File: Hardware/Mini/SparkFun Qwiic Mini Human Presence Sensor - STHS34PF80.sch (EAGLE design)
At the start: 29 parts, among them J1 Qwiic, J2 Qwiic, U2 STHS34PF80

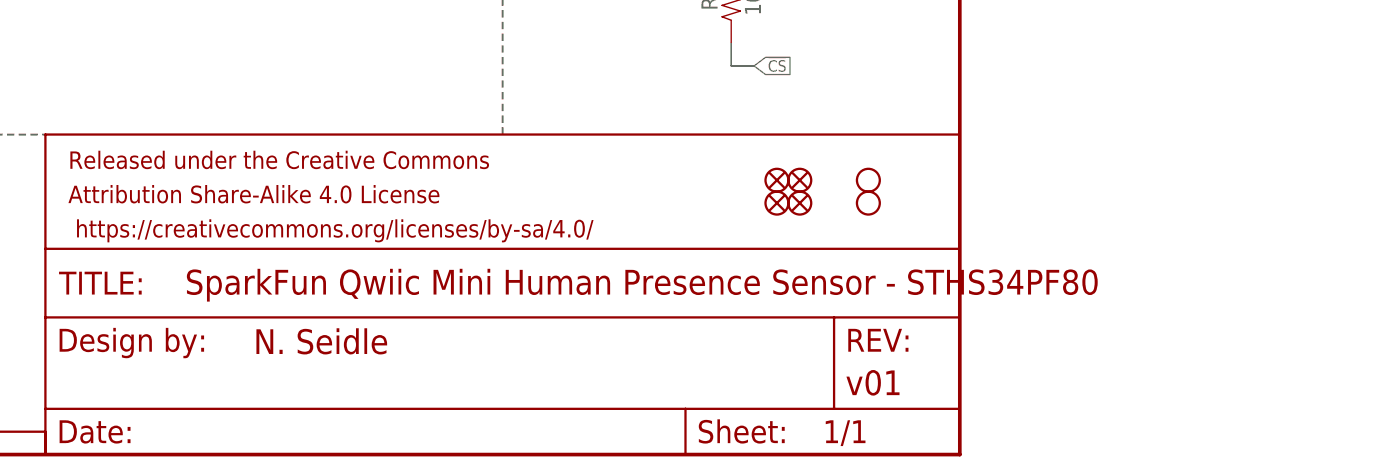
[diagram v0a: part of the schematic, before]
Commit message: Updated design for review and added production files for Mini
MINI ONLY: Completed layout and worked through design errors, panelized the board, and then created Gerbers for production. Added more comments throughout layout and schematic.
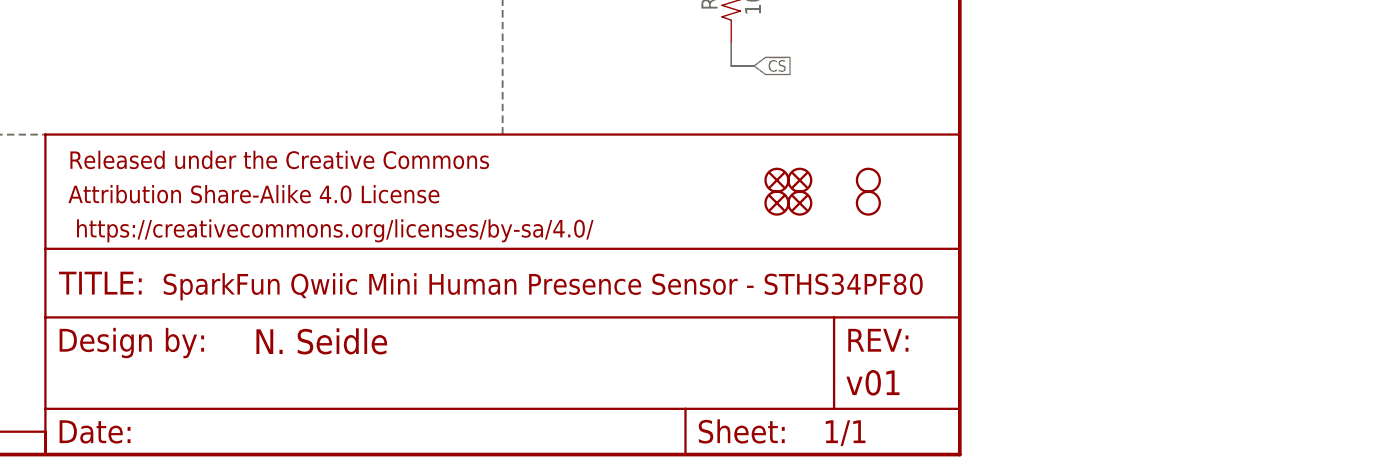
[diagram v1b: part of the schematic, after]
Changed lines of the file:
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@@
 <attribute name="LAST_DATE_TIME" x="160.02" y="1.27" size="2.54" layer="94" font="vector"/>
 <attribute name="SHEET" x="233.68" y="1.27" size="2.54" layer="94" font="vector"/>
-<attribute name="DRAWING_NAME" x="162.814" y="17.78" size="2.7432" layer="94" font="vector"/>
+<attribute name="DRAWING_NAME" x="160.274" y="17.78" size="2.286" layer="94" font="vector"/>
 <attribute name="DESIGNER" x="170.434" y="11.176" size="2.7432" layer="94" font="vector"/>
 <attribute name="REV" x="236.22" y="6.604" size="2.7432" layer="94" font="vector"/>

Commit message: Updated version number on schematic
Board is now ready for review
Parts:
- FRAME1: REV v01 -> v10
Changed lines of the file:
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@@
 <part name="FRAME1" library="SparkFun-Aesthetics" deviceset="FRAME-LETTER" device="">
 <attribute name="DESIGNER" value="N. Seidle"/>
-<attribute name="REV" value="v01"/>
+<attribute name="REV" value="v10"/>
 </part>
 <part name="LOGO5" library="SparkFun-Aesthetics" deviceset="SPECIAL_INSTRUCTIONS" device="-ORDERING"/>

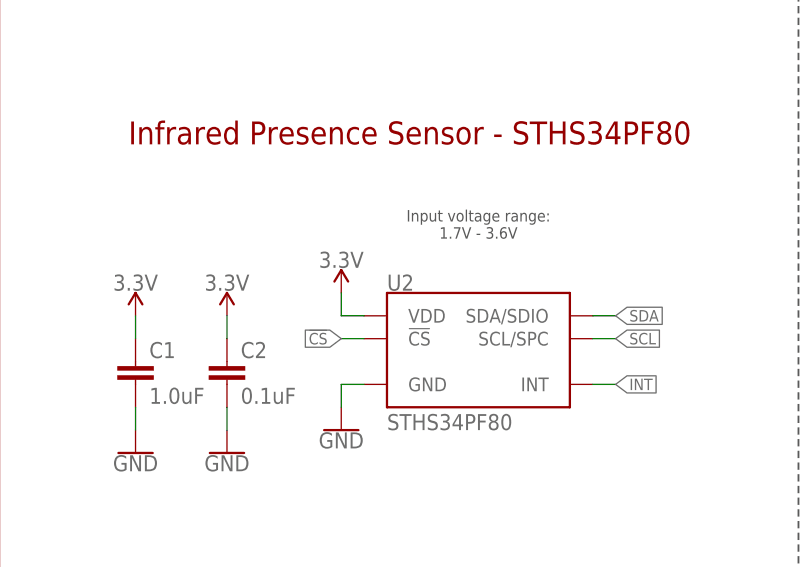
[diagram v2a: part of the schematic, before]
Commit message: Updated files for design review
Changed ST part to have 80% solder cream; changed panels to be 6x6 boards; changed vector font issues in schematic; added measures; added some more silk for easier part identification
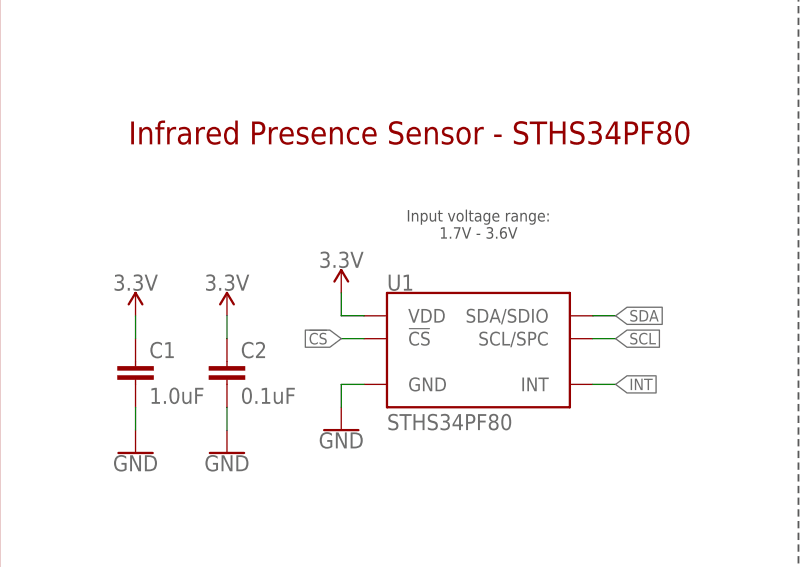
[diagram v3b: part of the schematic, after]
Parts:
- U1: PROD_ID (none) -> IC-19626
- renumbered U2 to U1

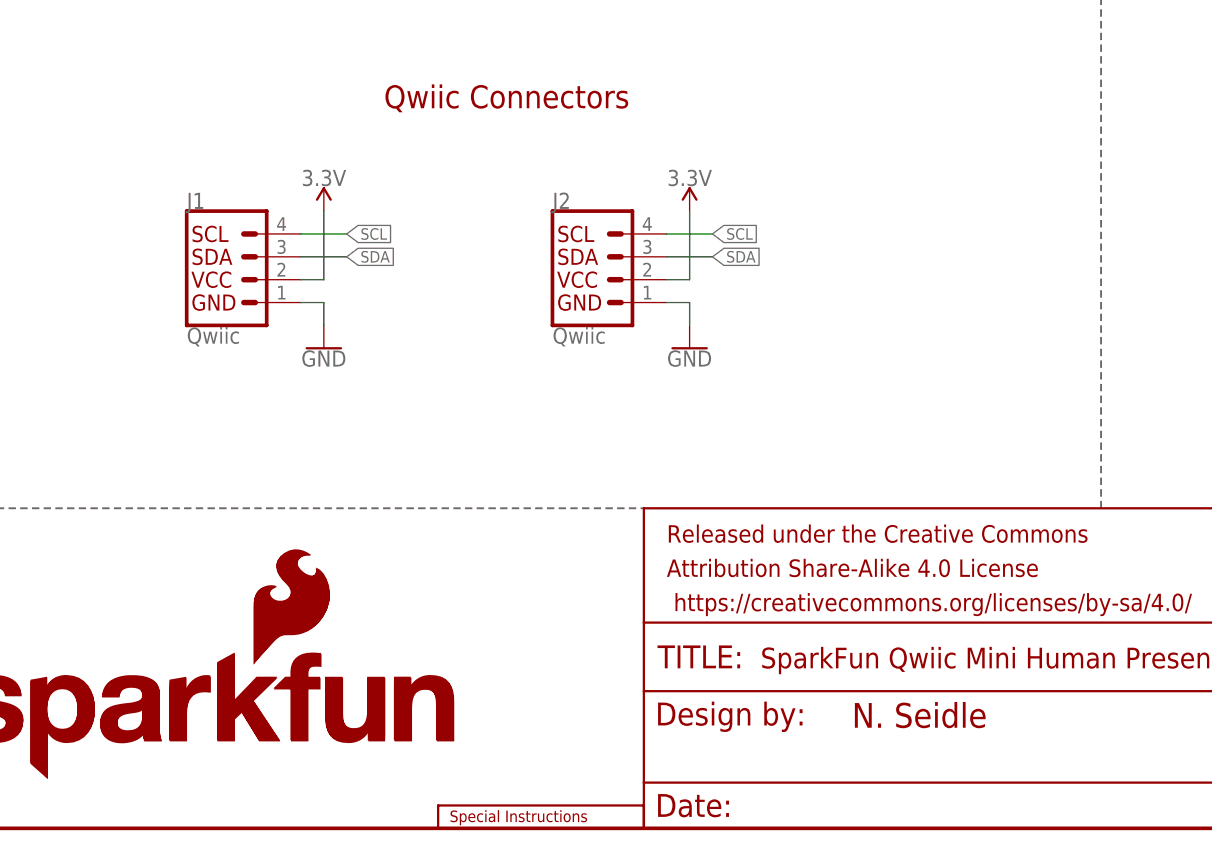
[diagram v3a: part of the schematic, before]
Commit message: Changed from Qwiic horizontal to qwiic vertical
Changed to the Qwiic Vertical connector we have for a better surface mounting option for the user. Updated the gerbers and panel to now have the correct information
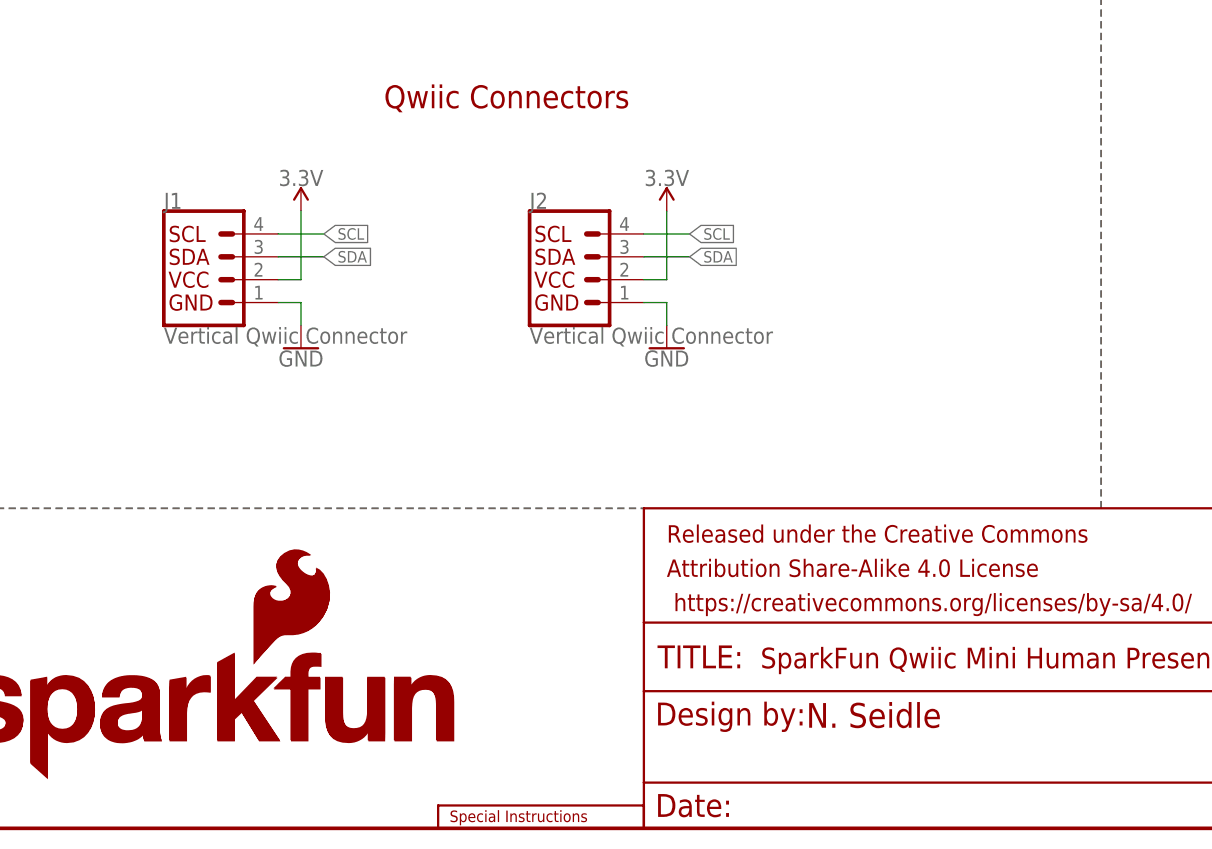
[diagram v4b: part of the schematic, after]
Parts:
- J1, J2: value Qwiic -> Vertical Qwiic Connector; device SparkFun-Connectors:QWIIC_CONNECTORJS-1MM -> SparkFun-Connectors:QWIIC_CONNECTOR

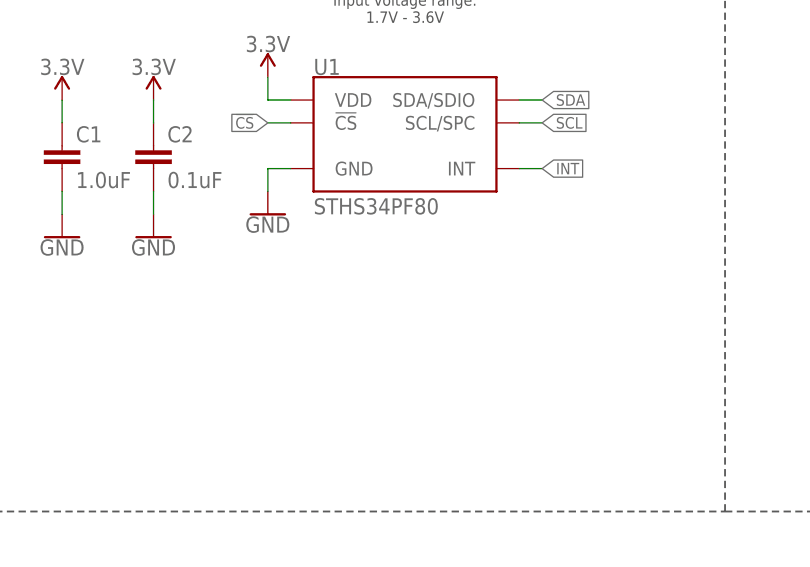
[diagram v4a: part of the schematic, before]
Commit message: Small documentation additions
Added I2C address to schematic and units for measures (measures in inches)
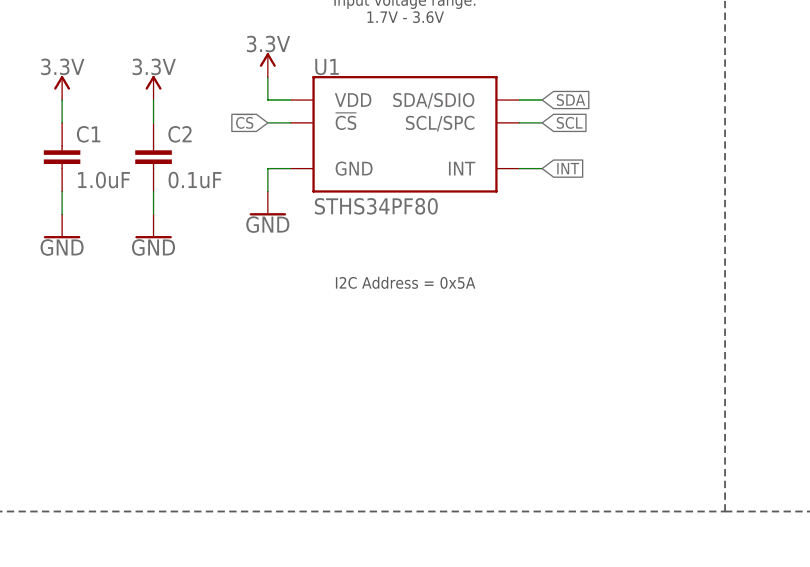
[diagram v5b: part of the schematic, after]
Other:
- note added: "I2C Address = 0x5A"
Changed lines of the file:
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@@
 <text x="118.364" y="141.986" size="2.032" layer="97" font="vector">I2C</text>
 <text x="228.092" y="62.23" size="2.032" layer="97" font="vector" rot="R90">!CS</text>
+<text x="53.34" y="119.38" size="1.27" layer="97" font="vector" align="center">I2C Address = 0x5A</text>
 </plain>
 <instances>
